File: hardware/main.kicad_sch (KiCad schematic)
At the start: 0 parts

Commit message: Full Schematic
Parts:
- added H1: HV+, symbol Mechanical:MountingHole_Pad
- added H2: HV-, symbol Mechanical:MountingHole_Pad
- added J1: SD+ GND, symbol Connector:Conn_01x03_Socket
- added J2: TSMP+ TSMP-, symbol Connector:Conn_01x03_Socket
- added K1: DBR72410, DBR72410, symbol Imported_Footprints_DISCHARGE:DBR72410
- added R1, R2: 4000, symbol Device:R
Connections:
- new net: J1.2 (Pin_2), K1.2 (NC)
- new net: H1.1, J2.1 (Pin_1), R2.1
- new net: R1.1, R2.2
- new net: K1.4 (COIL+), R1.2
- new net: H2.1, J2.3 (Pin_3), K1.3 (COIL-)
- new net GND: J1.3 (Pin_3), K1.1 (COM)
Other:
- note added: "40W"
- note added: "Strain relief"
- note added: "x ??"

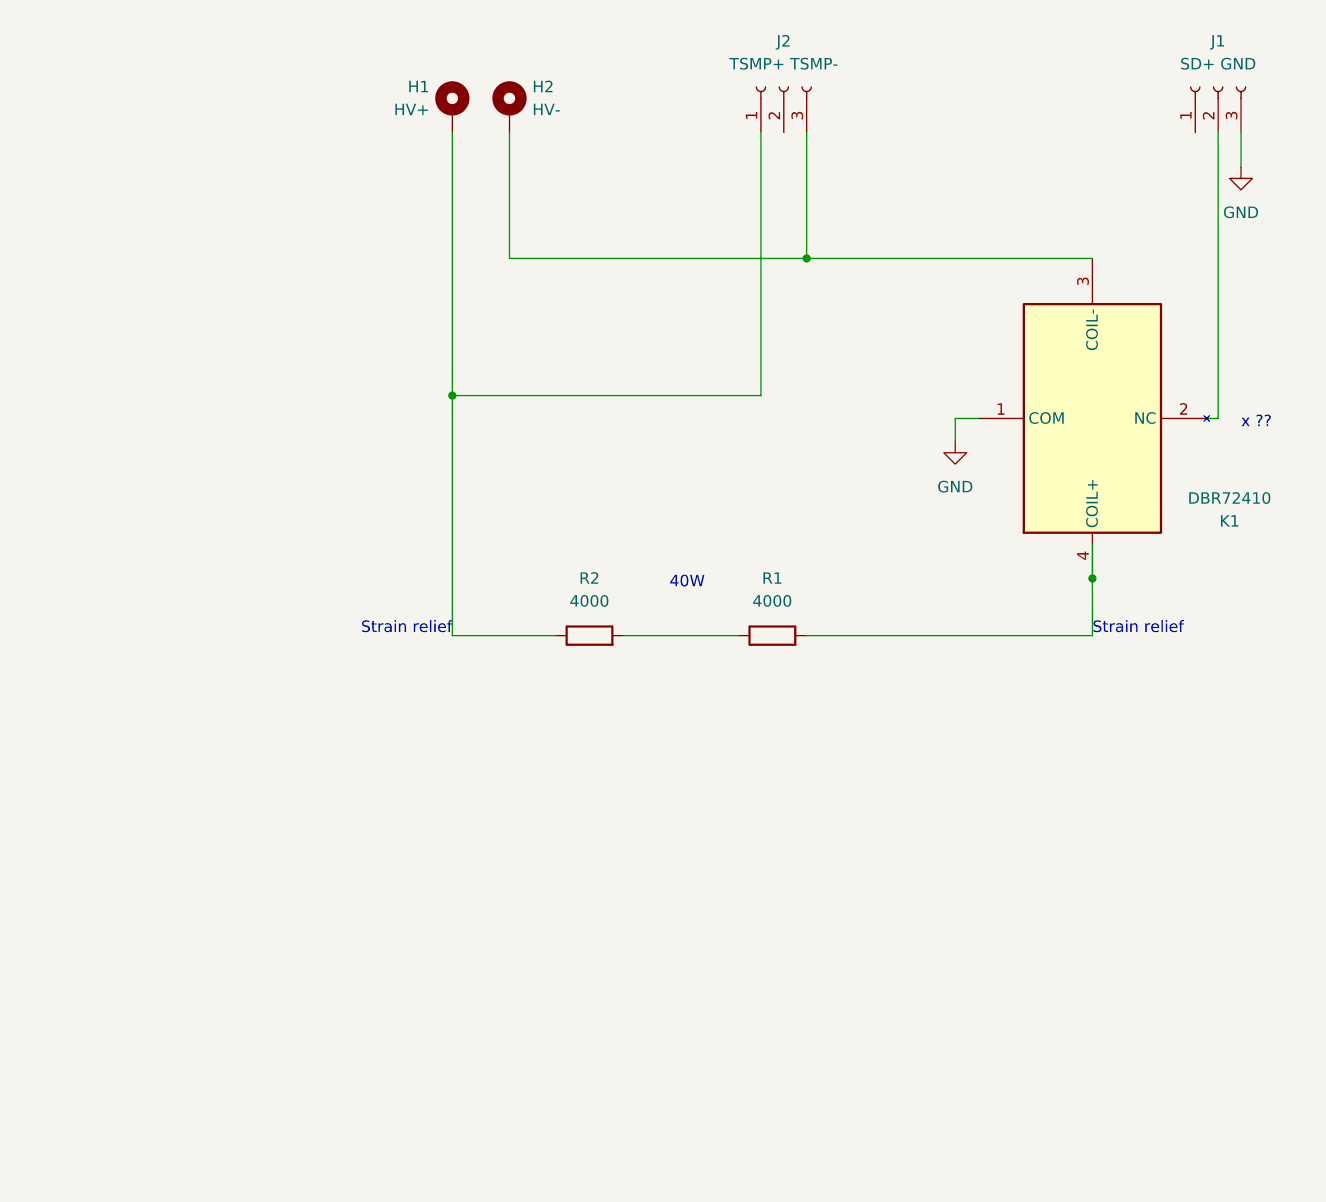
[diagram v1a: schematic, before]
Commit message: add connectors and change through hole for HV
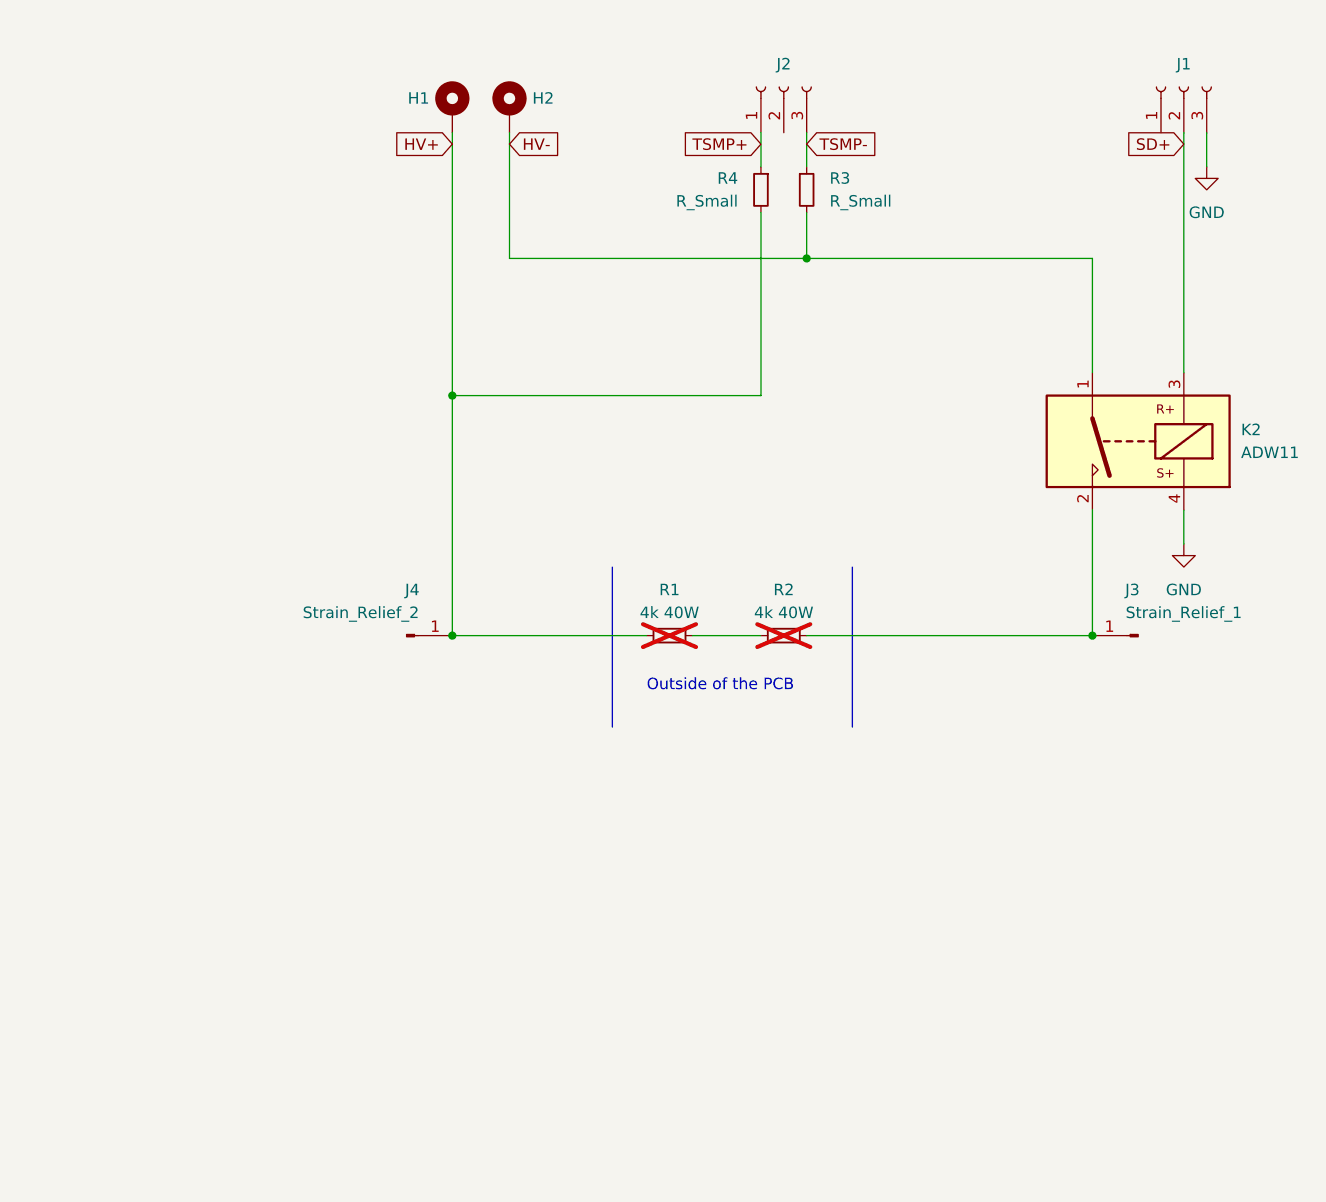
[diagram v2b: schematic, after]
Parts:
- removed K1: DBR72410, DBR72410, symbol Imported_Footprints_DISCHARGE:DBR72410
- removed R1, R2: 4000, symbol Device:R
- added J3: Strain_Relief_1, Connector_Wire:SolderWire-1.5sqmm_1x01_D1.7mm_OD3.9mm_Relief, symbol Connector:Conn_01x01_Pin
- added J4: Strain_Relief_2, Connector_Wire:SolderWire-1.5sqmm_1x01_D1.7mm_OD3.9mm_Relief, symbol Connector:Conn_01x01_Pin
- added K2: ADW11, KiCad:DBR72410, symbol Relay:ADW11
- added R1, R2: 4k 40W, symbol Device:R_Small
- added R3, R4: R_Small, TKH45P5K00FE-TR:TKH45P50R0FETR, symbol Device:R_Small
- H1: value HV+ -> ~; footprint (none) -> Connector_Wire:SolderWire-1.5sqmm_1x01_D1.7mm_OD3.9mm
- H2: value HV- -> ~; footprint (none) -> Connector_Wire:SolderWire-1.5sqmm_1x01_D1.7mm_OD3.9mm
- J1: value SD+ GND -> ~
- J2: value TSMP+ TSMP- -> ~
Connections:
- net GND: now also K2.4
- net SD+: now reaches J1.2 (Pin_2)
- net SD+: now also K2.3
- net HV+: now reaches H1.1
- net HV+: now also J4.1 (Pin_1), R1.1, R4.2; no longer J2.1 (Pin_1)
- net HV-: now reaches H2.1
- net HV-: now also K2.1, R3.2; no longer J2.3 (Pin_3)
- new net: J3.1 (Pin_1), K2.2, R2.2
- new net: R1.2, R2.1
- new net TSMP+: J2.1 (Pin_1), R4.1
- new net TSMP-: J2.3 (Pin_3), R3.1
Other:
- note added: "Outside of the PCB"
- note removed: "40W"
- note removed: "Strain relief"
- note removed: "x ??"
- moved on the sheet: J1

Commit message: changed Resistors and HV Cables
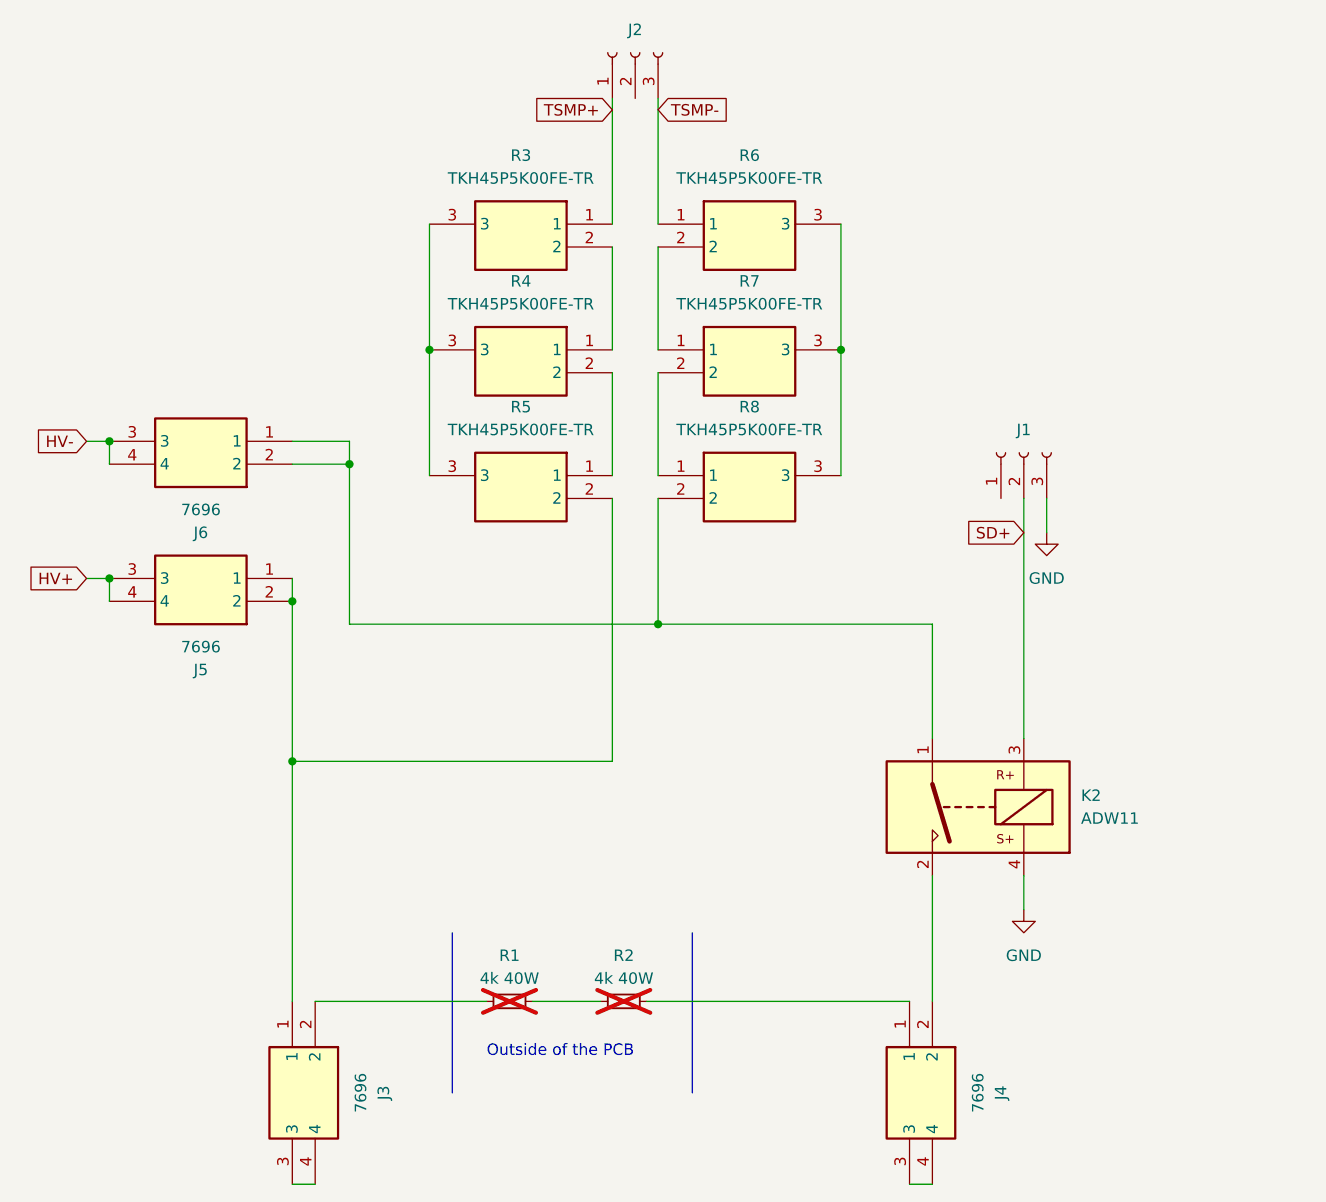
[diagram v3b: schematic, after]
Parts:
- removed H1, H2: ~, Connector_Wire:SolderWire-1.5sqmm_1x01_D1.7mm_OD3.9mm, symbol Mechanical:MountingHole_Pad
- removed J3: Strain_Relief_1, Connector_Wire:SolderWire-1.5sqmm_1x01_D1.7mm_OD3.9mm_Relief, symbol Connector:Conn_01x01_Pin
- removed J4: Strain_Relief_2, Connector_Wire:SolderWire-1.5sqmm_1x01_D1.7mm_OD3.9mm_Relief, symbol Connector:Conn_01x01_Pin
- removed R3, R4: R_Small, TKH45P5K00FE-TR:TKH45P50R0FETR, symbol Device:R_Small
- added J3, J4, J5, J6: 7696, 7696, symbol 7696:7696
- added R3, R4, R5, R6, R7, R8: TKH45P5K00FE-TR, TKH45P50R0FETR, symbol TKH45P5K00FE-TR:TKH45P5K00FE-TR
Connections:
- net HV+: now also J5.3, J5.4; no longer R1.1
- net HV-: now also J6.3, J6.4; no longer K2.1
- net TSMP+: now also R3.1
- net TSMP-: now also R6.1
- net at R2.2: now also J4.1; no longer K2.2
- new net: J3.1, J5.1, J5.2, R5.2
- new net: J3.2, R1.1
- new net: J3.3, J3.4
- new net: R3.2, R4.1
- new net: R4.2, R5.1
- new net: R3.3, R4.3, R5.3
- new net: R6.2, R7.1
- new net: R6.3, R7.3, R8.3
- new net: R7.2, R8.1
- new net: J4.2, K2.2
- new net: J4.3, J4.4
- new net: J6.1, J6.2, K2.1, R8.2
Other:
- moved on the sheet: J1, J2, K2, R1, R2

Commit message: Still have to take the measurements
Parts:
- removed J3, J4, J5, J6: 7696, 7696, symbol 7696:7696
- added J3, J4, J5, J6: Conn_01x01_Pin, 7696:7696, symbol Connector:Conn_01x01_Pin
- J1, J2: footprint (none) -> d369-g33-xx:D369-G33-XX
- R3, R4, R5, R6, R7, R8: footprint TKH45P50R0FETR -> TKH45P5K00FE-TR:TKH45P50R0FETR
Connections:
- net HV+: now also R1.1, R5.2, J3.1 (Pin_1), J6.1 (Pin_1)
- net HV-: now also K2.1, R8.2, J5.1 (Pin_1)
- net at R2.2: now also K2.2, J4.1 (Pin_1)
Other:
- moved on the sheet: J2

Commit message: Added calculations
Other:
- company: Author: -> Author: Marco W. Santoro
- title: (none) -> Discharge
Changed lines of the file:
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@@
   (paper "A4")
   (title_block
+    (title "Discharge")
     (rev "${REVISION}")
-    (company "Author:")
+    (company "Author: Marco W. Santoro")
     (comment 1 "Reviewer:")
   )
